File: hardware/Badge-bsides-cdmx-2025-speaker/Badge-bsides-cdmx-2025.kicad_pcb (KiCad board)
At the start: 2 copper layers, 50 x 110 mm, 30 parts, among them J1 SWDIO, J3 ADDON, J4 Conn_01x04_Pin, J5 I2C, J6 Conn_01x04_Pin, P6 USB_C_Plug_USB2.0, Q3 DMG3415U-7, SW11 ON, SW2 RESET, U1 PY32F030F28U6TR, U6 AP2112K-3.3

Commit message: feat(Hw):started_routing
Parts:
- added C67: 10uF, Capacitor_SMD:C_0603_1608Metric, B.Cu at (153.0, 82.3)
- added C68: 10uF, Capacitor_SMD:C_0603_1608Metric, B.Cu at (143.4, 82.3)
- added C69: 10uF, Capacitor_SMD:C_0603_1608Metric, B.Cu at (133.8, 82.4)
- added C70: 10uF, Capacitor_SMD:C_0603_1608Metric, B.Cu at (124.0, 83.7)
- added R5: 10k, Resistor_SMD:R_0603_1608Metric, B.Cu at (153.0, 83.8)
- added R6: 10k, Resistor_SMD:R_0603_1608Metric, B.Cu at (143.4, 83.8)
- added R7: 10k, Resistor_SMD:R_0603_1608Metric, B.Cu at (133.8, 83.9)
- added R8: 10k, Resistor_SMD:R_0603_1608Metric, B.Cu at (124.0, 82.2)
- added SW10: SW_Push, Footprints:TS1088R02026, F.Cu at (124.1, 82.9)
- added SW7: SW_Push, Footprints:TS1088R02026, F.Cu at (133.8, 83.0)
- added SW8: SW_Push, Footprints:TS1088R02026, F.Cu at (152.9, 82.9)
- added SW9: SW_Push, Footprints:TS1088R02026, F.Cu at (143.4, 83.0)
- BT3, BT4, J4: moved to B.Cu
- J3, J5: moved to F.Cu
- moved J1 59.8 mm to (116.3, 60.7)
- moved J3 41.3 mm to (119.3, 40.3), turned to 90 degrees
- moved BT3 37.9 mm to (160.5, 123.0), turned to 180 degrees
- moved BT4 34.0 mm to (160.5, 137.1), turned to 180 degrees
- moved SW2 32.7 mm to (126.7, 94.2)
- moved R4 32.7 mm to (131.8, 92.7)
- moved C6 32.7 mm to (123.9, 90.4)
- moved J5 19.6 mm to (116.1, 69.1), turned to 0 degrees
- moved R11 16.3 mm to (148.0, 56.4), turned to 180 degrees
- moved R9 14.0 mm to (133.2, 110.6), turned to 0 degrees
- moved D9 13.5 mm to (134.1, 113.4), turned to 0 degrees
- moved C33 13.3 mm to (151.2, 99.6)
- moved D10 13.3 mm to (147.7, 59.9)
- moved F3 12.7 mm to (151.2, 102.6)
- moved J4 12.6 mm to (160.2, 84.6), turned to 180 degrees
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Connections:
- BT3 pad 2: +3.3V -> +BATT
- J3 pad 5: /GPIO1 -> /GPIO2
- J3 pad 6: /GPIO2 -> /GPIO1
- U1 pad 1: unconnected-(U1-PA5-Pad1) -> /BTTN2
- U1 pad 10: unconnected-(U1-PB6-Pad10) -> /LED1
- U1 pad 16: /GPIO2 -> /BTTN4
- U1 pad 17: /GPIO1 -> /BTTN3
- U1 pad 2: /LED1 -> /BTTN1
- U1 pad 20: unconnected-(U1-PA4-Pad20) -> /LED2
- U1 pad 3: /LED2 -> /GPIO1
- U1 pad 5: unconnected-(U1-PA12-Pad5) -> /GPIO2
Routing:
- net Net-(BT3--): track 0.00 -> 55.1 mm
- net VBUS: track 0.00 -> 40.2 mm, vias 0 -> 2
- net +BATT: track 0.00 -> 16.9 mm
- net Net-(SW11-A): track 0.00 -> 14.8 mm
- net Net-(F3-Pad1): track 0.00 -> 10.8 mm
- net Net-(D4-K): track 0.00 -> 9.51 mm
- net Net-(P6-CC): track 0.00 -> 7.73 mm
- net Net-(P6-VCONN): track 0.00 -> 6.86 mm
- net /TX: track 0.00 -> 2.54 mm
- net /RX: track 0.00 -> 2.54 mm
- net +3V3: track 0.00 -> 1.80 mm
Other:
- board size 50 x 110 mm -> 50.1 x 110 mm

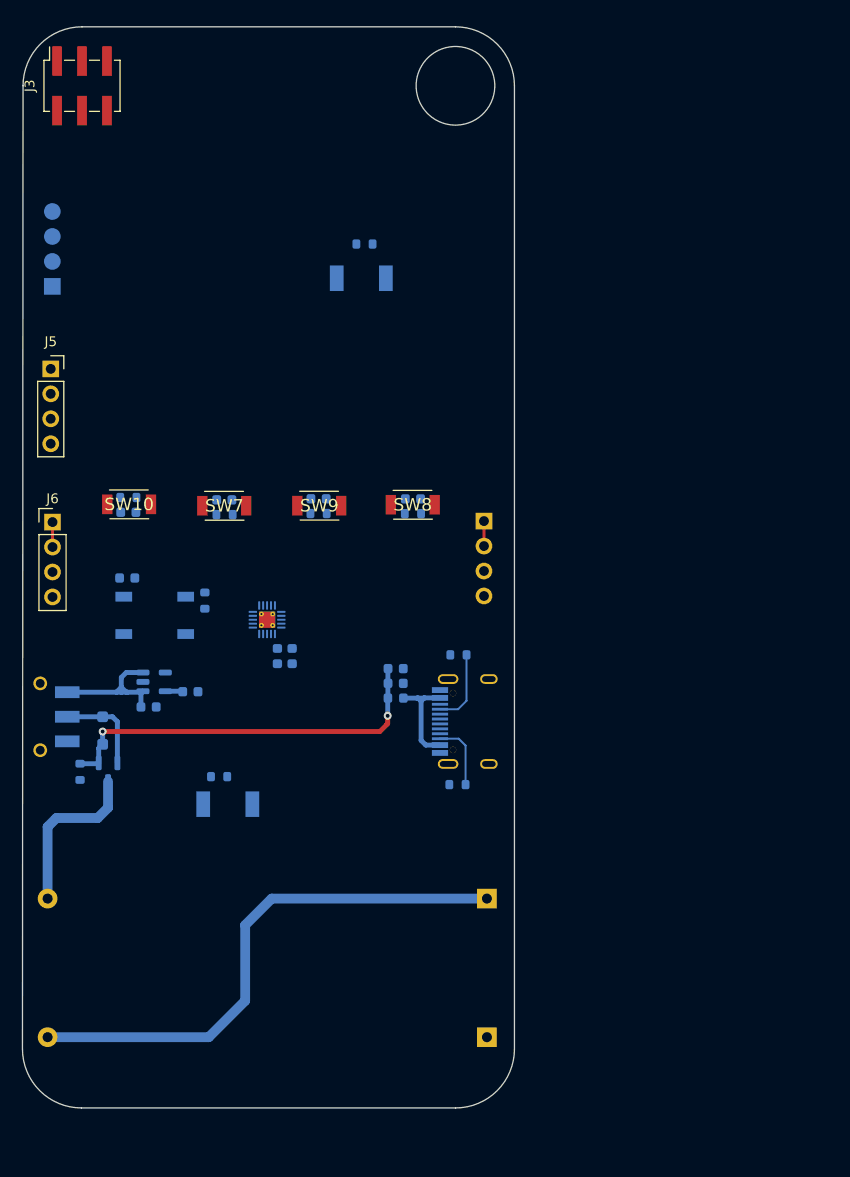
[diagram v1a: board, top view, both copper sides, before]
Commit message: feat(Hw):Route_Sponsor
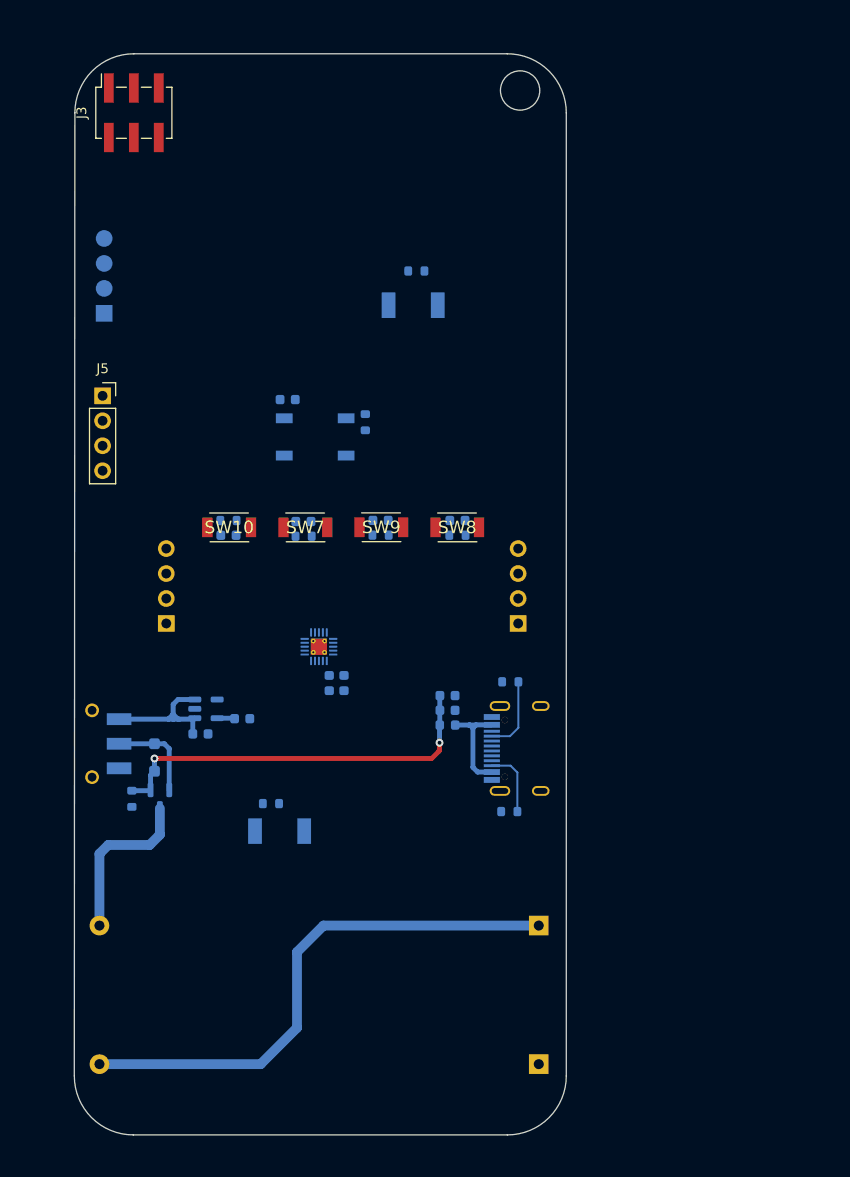
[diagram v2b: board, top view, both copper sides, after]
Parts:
- J4: footprint Connector_PinHeader_2.54mm:PinHeader_1x04_P2.54mm_Vertical -> Connector_PinHeader_2.54mm:PinHeader_1x04_P2.54mm_Horizontal
- J6: footprint Connector_PinHeader_2.54mm:PinHeader_1x04_P2.54mm_Vertical -> Connector_PinSocket_2.54mm:PinSocket_1x04_P2.54mm_Horizontal; moved to B.Cu
- moved C6 24.4 mm to (140.2, 72.2)
- moved R4 24.4 mm to (148.1, 74.5)
- moved SW2 24.4 mm to (143.0, 76.0)
- moved J6 15.5 mm to (127.9, 95.0)
- moved J4 11.0 mm to (163.7, 95.0), turned to 0 degrees
- moved C70 10.5 mm to (134.2, 86.0)
- moved R8 10.5 mm to (134.2, 84.5)
- moved SW10 10.5 mm to (134.3, 85.2)
- moved SW7 8.54 mm to (142.0, 85.2)
- moved C69 8.34 mm to (141.8, 84.6)
- moved R7 8.34 mm to (141.9, 86.1)
- moved SW9 6.68 mm to (149.8, 85.2)
- moved C68 6.68 mm to (149.7, 84.5)
- moved R6 6.68 mm to (149.7, 86.0)
- moved BT3 5.95 mm to (165.8, 125.7)
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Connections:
- J4 pad 1: /RX -> GND
- J4 pad 2: /RX -> GND
- J4 pad 3: GND -> /RX
- J4 pad 4: GND -> /RX
- J6 pad 1: /TX -> GND
- J6 pad 2: /TX -> GND
- J6 pad 3: GND -> /TX
- J6 pad 4: GND -> /TX
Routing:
- net /TX: track 2.54 -> 0.00 mm
- net /RX: track 2.54 -> 0.00 mm
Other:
- outline, holes or cut-outs redrawn

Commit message: feat(Hw):Update_BOM_And_Route
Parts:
- removed D10, D9: R_LED, Footprints:LYT77K-K2M1
- removed R11, R9: 220, Resistor_SMD:R_0603_1608Metric
- added C29: 100nF, Capacitor_SMD:C_0603_1608Metric, F.Cu at (193.7, 42.0)
- added C30: 100nF, Capacitor_SMD:C_0603_1608Metric, F.Cu at (193.7, 44.5)
- added D19: WS2812B, Footprints:LED_SK6812-E, B.Cu at (153.6, 62.8)
- added D20: WS2812B, Footprints:LED_SK6812-E, B.Cu at (140.3, 116.9)
- added J4: OLED, bsides:Display OLED 128 x32, F.Cu at (126.3, 68.0)
- added R3: 1K, Resistor_SMD:R_0603_1608Metric, F.Cu at (193.7, 47.0)
- moved BT3 44.5 mm to (121.3, 125.7), turned to 0 degrees
- moved SW2 28.7 mm to (159.9, 52.8), turned to 180 degrees
- moved C6 27.4 mm to (162.7, 56.6), turned to 180 degrees
- moved R4 21.3 mm to (154.8, 54.3), turned to 90 degrees
- moved J5 6.21 mm to (126.3, 68.0)
- moved J1 4.32 mm to (122.0, 59.2)
- moved BT4 0.13 mm to (165.9, 139.8)
- moved C67 0.09 mm to (157.4, 84.5)
- moved R5 0.09 mm to (157.4, 86.0)
- moved SW9 0.09 mm to (149.7, 85.2)
- moved C68 0.09 mm to (149.6, 84.5)
- moved C69 0.09 mm to (141.7, 84.6)
- moved C70 0.09 mm to (134.1, 86.0)
- moved R6 0.09 mm to (149.6, 86.0)
- moved R7 0.09 mm to (141.8, 86.1)
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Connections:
- C26 pad 1: +3V3 -> +3.3V
- J3 pad 1: +3V3 -> +3.3V
- J4 pad 3: /RX -> /TX
- J4 pad 4: /RX -> /TX
- J6 pad 3: /TX -> /RX
- J6 pad 4: /TX -> /RX
- R4 pad 2: +3V3 -> +3.3V
- R5 pad 2: +3V3 -> +3.3V
- R6 pad 2: +3V3 -> +3.3V
- R7 pad 2: +3V3 -> +3.3V
- R8 pad 2: +3V3 -> +3.3V
- U1 pad 10: /LED1 -> unconnected-(U1-PB6-Pad10)
- U1 pad 11: unconnected-(U1-PB7-Pad11) -> /GPIO1
- U1 pad 12: unconnected-(U1-PF4/BOOT0-Pad12) -> /GPIO2
- U1 pad 20: /LED2 -> unconnected-(U1-PA4-Pad20)
- U1 pad 3: /GPIO1 -> /NEO
- U1 pad 5: /GPIO2 -> unconnected-(U1-PA12-Pad5)
- U6 pad 5: +3V3 -> +3.3V
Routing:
- net Net-(BT3--): track 55.1 -> 0.00 mm
- net +BATT: track 16.9 -> 9.63 mm
- net +3V3: track 1.80 -> 0.00 mm
- net +3.3V: track 0.00 -> 1.80 mm
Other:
- board size 50.1 x 110 mm -> 49.9 x 109.8 mm

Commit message: feat(Hw):Update_Route
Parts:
- removed C10, C26, C27: 10uF, Capacitor_SMD:C_0603_1608Metric
- removed C33: 100nF, Capacitor_SMD:C_0603_1608Metric
- removed D4: MBR120, Diode_SMD:D_SOD-123F
- removed F3: 750mA, Fuse:Fuse_0603_1608Metric
- removed the J4 at (126.3, 68.0)
- removed P6: USB_C_Plug_USB2.0, Footprints:C393939
- removed Q3: DMG3415U-7, Package_TO_SOT_SMD:SOT-23
- removed R10: 100K, Resistor_SMD:R_0603_1608Metric
- removed R41, R45: 5k1, Resistor_SMD:R_0603_1608Metric
- removed U6: AP2112K-3.3, Package_TO_SOT_SMD:SOT-23-5
- C29, C30, R3: moved to B.Cu
- moved C30 93.1 mm to (135.2, 116.9), turned to -90 degrees
- moved J1 63.4 mm to (165.9, 104.9), turned to 180 degrees
- moved C29 49.8 mm to (148.4, 62.8), turned to -90 degrees
- moved R3 38.2 mm to (158.9, 62.8), turned to 90 degrees
- moved C6 3.26 mm to (165.1, 54.3), turned to 90 degrees
- moved R7 1.50 mm to (141.8, 84.6)
- moved R6 1.50 mm to (149.6, 84.5)
- moved C69 1.46 mm to (141.7, 86.1)
- moved C68 1.45 mm to (149.6, 85.9)
- moved J4 0.62 mm to (164.3, 95.0)
- moved C34 0.41 mm to (144.9, 101.1)
- moved C28 0.37 mm to (146.3, 101.1)
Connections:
- J1 pad 1: VBUS -> +3.3V
- SW11 pad 2: Net-(D4-K) -> +BATT
- SW11 pad 3: Net-(SW11-A) -> +3.3V
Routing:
- net +3.3V: track 1.80 -> 250.2 mm, vias 0 -> 4
- net /GPIO2: track 0.00 -> 85.4 mm, vias 0 -> 1
- net Net-(D19-DOUT): track 0.00 -> 80.5 mm, vias 0 -> 4
- net /SDA: track 0.00 -> 79.6 mm
- net /SCL: track 0.00 -> 73.3 mm
- net /NTST: track 0.00 -> 72.0 mm, vias 0 -> 2
- net /GPIO1: track 0.00 -> 66.7 mm, vias 0 -> 1
- net +BATT: track 9.63 -> 59.7 mm
- net /NEO: track 0.00 -> 49.0 mm
- net VBUS: track 40.2 -> 0.00 mm, vias 2 -> 0
- net /SWCLK: track 0.00 -> 33.1 mm
- net /SWDIO: track 0.00 -> 30.2 mm
- net /TX: track 0.00 -> 29.7 mm, vias 0 -> 1
- net /BTTN1: track 0.00 -> 28.9 mm, vias 0 -> 1
- net /RX: track 0.00 -> 24.2 mm, vias 0 -> 2
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- added copper zone on B.Cu, net GND
- added copper zone on F.Cu, net GND

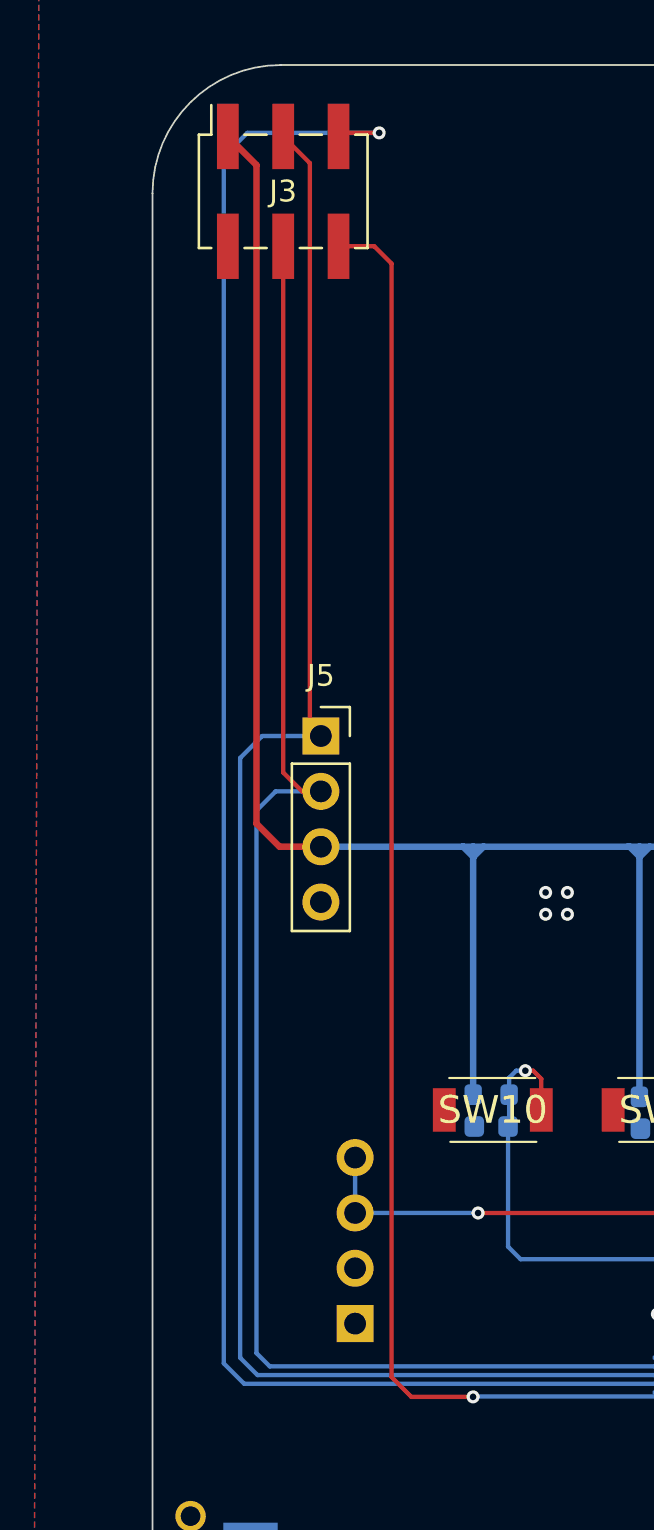
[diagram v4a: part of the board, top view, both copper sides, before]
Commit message: feat(Hw):Update_Labels
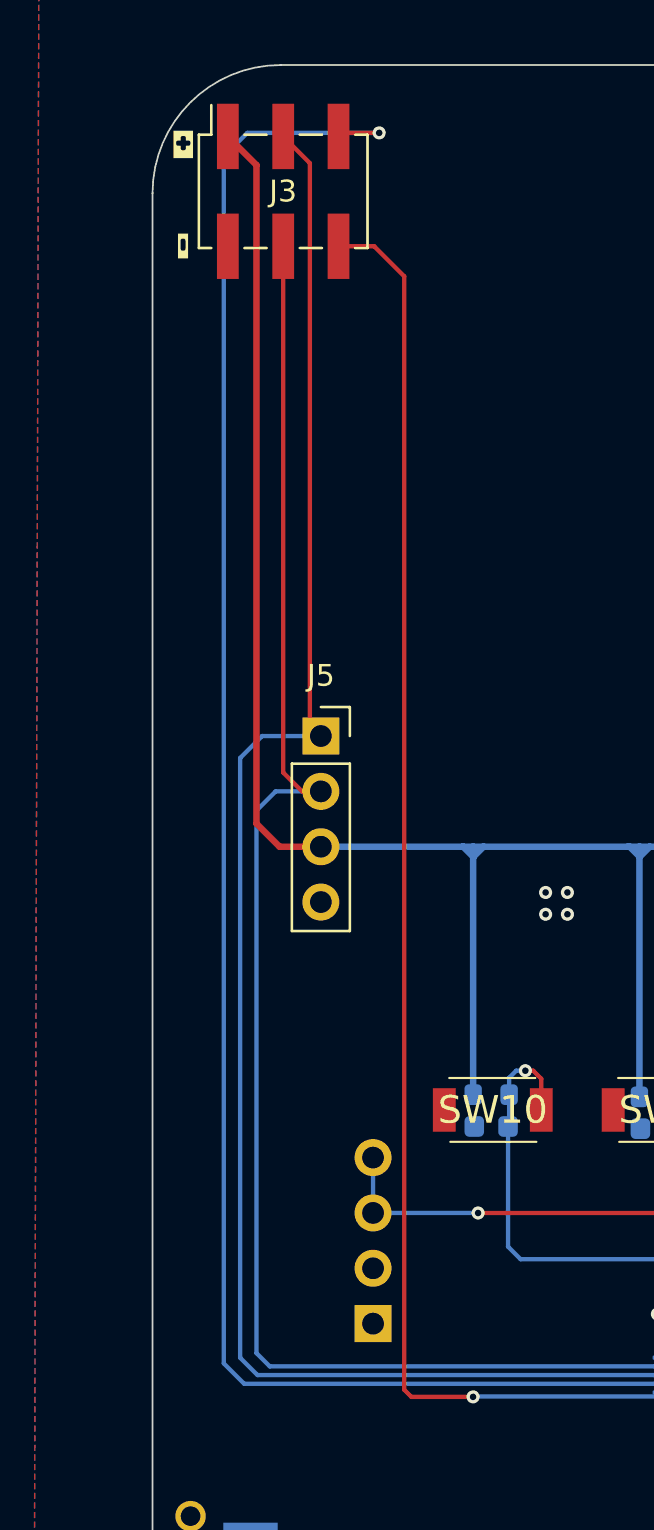
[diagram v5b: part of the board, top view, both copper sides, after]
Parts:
- added kibuzzard-6841DC13: G***, kibuzzard-6841DC13, B.Cu at (160.0, 56.6)
- added kibuzzard-6842ED2D: G***, kibuzzard-6842ED2D, B.Cu at (162.3, 104.9)
- added kibuzzard-6842ED45: G***, kibuzzard-6842ED45, B.Cu at (162.3, 112.5)
- added kibuzzard-6842EE28: G***, kibuzzard-6842EE28, F.Cu at (120.0, 40.9)
- added kibuzzard-6842EE36: G***, kibuzzard-6842EE36, F.Cu at (120.0, 45.5)
- added kibuzzard-684316CB: G***, kibuzzard-684316CB, B.Cu at (120.7, 101.8)
- added kibuzzard-684316D5: G***, kibuzzard-684316D5, B.Cu at (120.8, 112.8)
- added kibuzzard-68437E7E: G***, kibuzzard-68437E7E, B.Cu at (161.4, 110.0)
- added kibuzzard-68437EB0: G***, kibuzzard-68437EB0, B.Cu at (161.6, 107.5)
- moved J6 0.82 mm to (128.7, 95.0)
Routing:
- net /RX: track 24.2 -> 23.4 mm

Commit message: fix(Hw):Labels_Updated
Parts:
- D19, D20: value WS2812B -> SK6812MINI-E
- R3: value 1K -> 470R
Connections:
- U1 pad 21: (no net) -> GND
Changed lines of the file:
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@@
 			(fill yes)
 			(layer "F.SilkS")
-			(net 7864429)
 		)
 		(embedded_fonts no)
@@
 			(fill yes)
 			(layer "F.SilkS")
-			(net 7864429)
 		)
 		(embedded_fonts no)
@@
 			(layers "*.Cu")
 			(remove_unused_layers no)
+			(net 1 "GND")
+			(pinfunction "VSS")
+			(pintype "bidirectional")
 		)
 		(pad "21" thru_hole circle
@@
 			(layers "*.Cu")
 			(remove_unused_layers no)
+			(net 1 "GND")
+			(pinfunction "VSS")
+			(pintype "bidirectional")
 		)
 		(pad "21" smd rect
@@
 			(property pad_prop_heatsink)
 			(layers "F.Cu")
+			(net 1 "GND")
+			(pinfunction "VSS")
+			(pintype "bidirectional")
 			(zone_connect 2)
 		)
@@
 			(property pad_prop_heatsink)
 			(layers "B.Cu" "B.Mask")
+			(net 1 "GND")
+			(pinfunction "VSS")
+			(pintype "bidirectional")
 			(zone_connect 2)
 		)
@@
 			(layers "*.Cu")
 			(remove_unused_layers no)
+			(net 1 "GND")
+			(pinfunction "VSS")
+			(pintype "bidirectional")
 		)
 		(pad "21" thru_hole circle
@@
 			(layers "*.Cu")
 			(remove_unused_layers no)
+			(net 1 "GND")
+			(pinfunction "VSS")
+			(pintype "bidirectional")
 		)
 		(embedded_fonts no)
@@
 			)
 		)
-		(property "Value" "WS2812B"
+		(property "Value" "SK6812MINI-E"
 			(at 7.26 -3.17151 0)
 			(layer "B.Fab")
@@
 			)
 		)
-		(property "LCSC#" "C527089"
+		(property "LCSC#" "C5149201"
 			(at 0 0 0)
 			(unlocked yes)
@@
 			)
 		)
-		(property "Manufacturer_Part_Number" "WS2812B-Mini"
+		(property "Manufacturer_Part_Number" ""
 			(at 0 0 0)
 			(unlocked yes)
@@
 			)
 		)
-		(property "Value" "WS2812B"
+		(property "Value" "SK6812MINI-E"
 			(at 7.26 -3.17151 0)
 			(layer "B.Fab")
@@
 			)
 		)
-		(property "LCSC#" "C527089"
+		(property "LCSC#" "C5149201"
 			(at 0 0 0)
 			(unlocked yes)
@@
 			)
 		)
-		(property "Manufacturer_Part_Number" "WS2812B-Mini"
+		(property "Manufacturer_Part_Number" ""
 			(at 0 0 0)
 			(unlocked yes)
@@
 			(fill yes)
 			(layer "B.SilkS")
-			(net 7864429)
 		)
 		(embedded_fonts no)
@@
 				(font
 					(size 0.001 0.001)
+					(thickness 0.15)
 				)
 				(justify mirror)
@@
 				(font
 					(size 0.001 0.001)
+					(thickness 0.15)
 				)
 				(justify mirror)
@@
 				(font
 					(size 0.001 0.001)
+					(thickness 0.15)
 				)
 				(justify mirror)
@@
 				(font
 					(size 0.001 0.001)
+					(thickness 0.15)
 				)
 				(justify mirror)
@@
 			)
 		)
-		(property "LCSC#" "C478888"
+		(property "LCSC#" "C66501"
 			(at 0 0 90)
 			(unlocked yes)
@@
 			)
 		)
-		(property "LCSC#" "C478888"
+		(property "LCSC#" "C66501"
 			(at 0 0 90)
 			(unlocked yes)
@@
 			)
 		)
-		(property "LCSC#" "C14663"
+		(property "LCSC#" "C66501"
 			(at 0 0 90)
 			(unlocked yes)
@@
 			)
 		)
-		(property "LCSC#" "-"
+		(property "LCSC#" "C221660"
 			(at 0 0 270)
 			(unlocked yes)
@@
 			)
 		)
-		(property "Manufacturer_Part_Number" "JS102011SAQN"
+		(property "Manufacturer_Part_Number" ""
 			(at 0 0 270)
 			(unlocked yes)
@@
 			)
 		)
-		(property "LCSC#" "C14663"
+		(property "LCSC#" "C66501"
 			(at 0 0 270)
 			(unlocked yes)
@@
 			)
 		)
-		(property "Value" "1K"
+		(property "Value" "470R"
 			(at 0 -1.43 90)
 			(layer "B.Fab")
@@
 			)
 		)
-		(property "LCSC#" "C22548"
+		(property "LCSC#" "C114669"
 			(at 0 0 270)
 			(unlocked yes)
